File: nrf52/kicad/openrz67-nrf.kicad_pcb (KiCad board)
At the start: 2 copper layers, 27 x 29 mm, 13 parts, among them J1 Camera, J2 SWD, SW1 B3U-1000P, U1 E73-2G4M08S1C, U2 TLP172AM, U3 TLP172AM

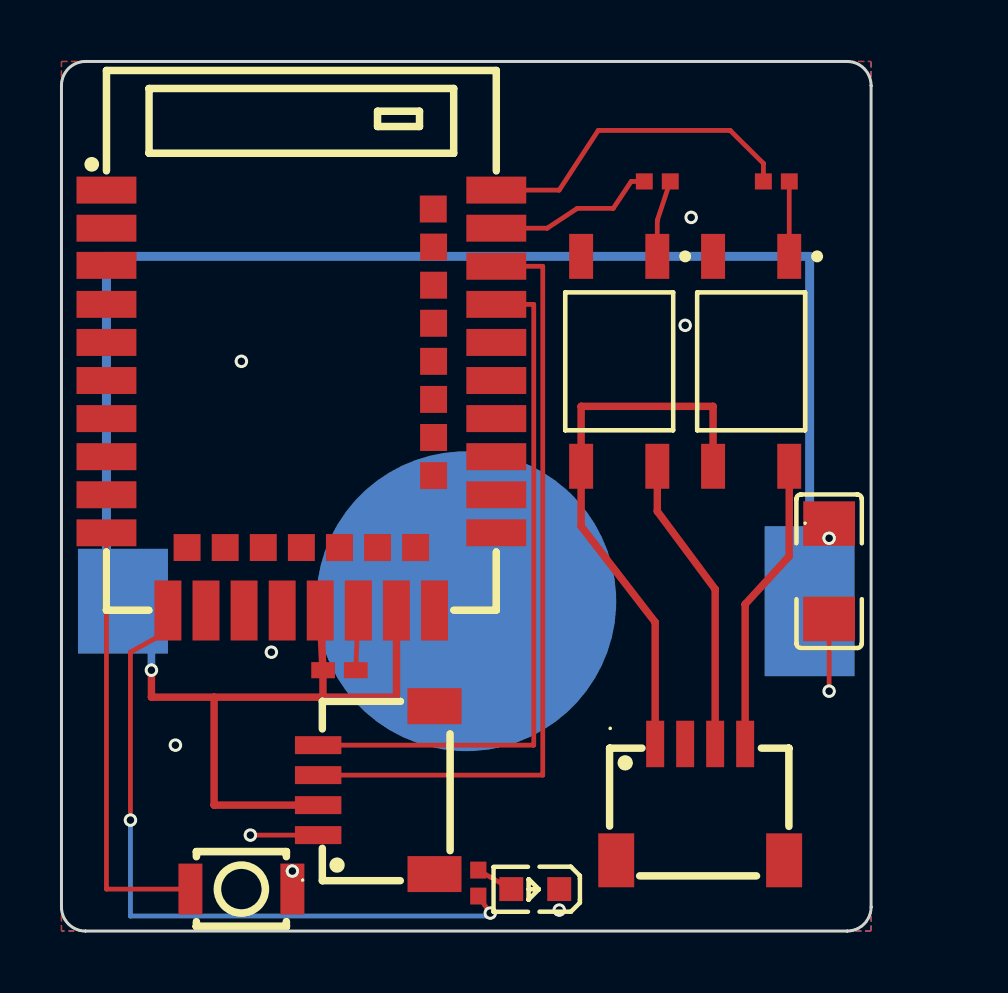
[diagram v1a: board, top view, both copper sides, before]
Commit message: nrf52: no paste on cell pad, VBUS to GND, vias out of pads
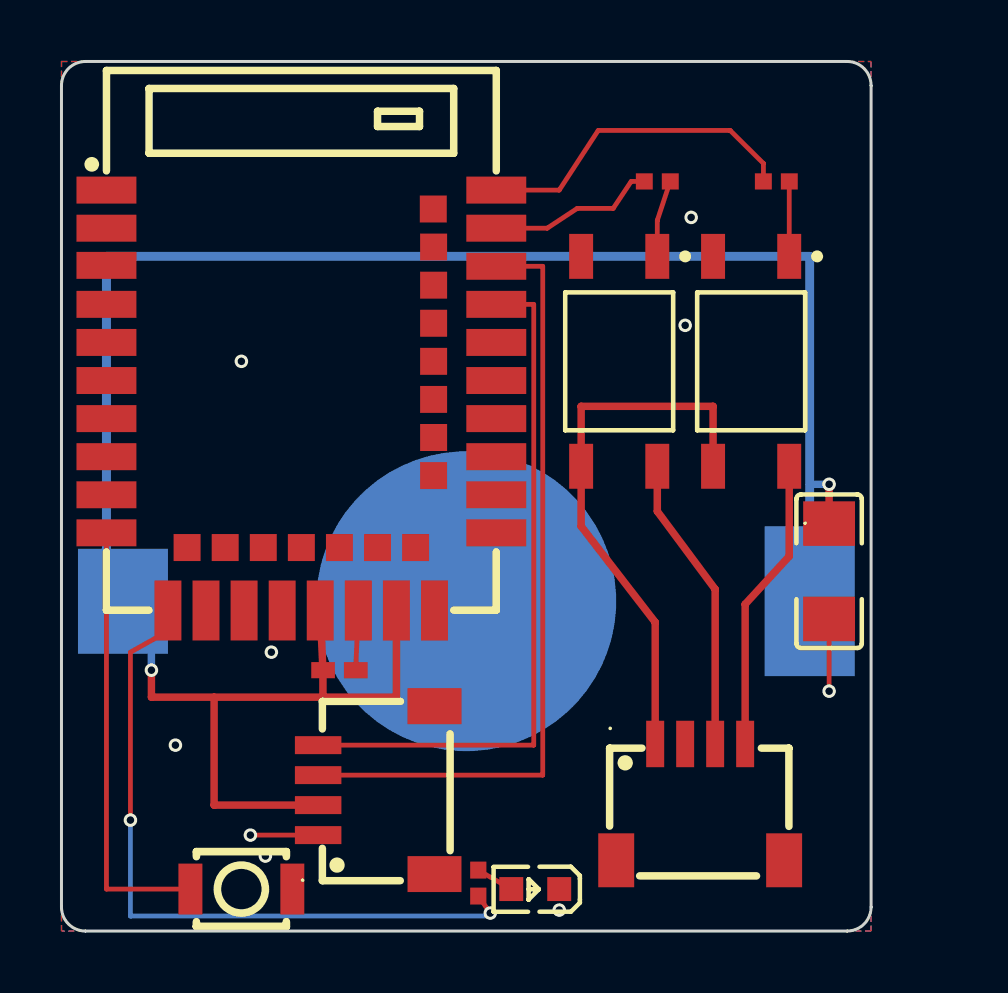
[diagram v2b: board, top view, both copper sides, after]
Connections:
- U1 pad 27: unconnected-(U1-VBS-Pad27) -> GND
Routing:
- net VDD: track 65.7 -> 67.2 mm

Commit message: nrf52 pcb: cell polarity label on the back silkscreen
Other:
- board text added: "CR2032 + SIDE OUT"

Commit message: nrf52 pcb: basic C2, R3 shares the 330 Ω part
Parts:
- R3: value 1kΩ -> 330Ω

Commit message: nrf52 pcb: connector names and board name on silkscreen
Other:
- board text added: "CAM"
- board text added: "OpenRZ67 nRF rev A"
- board text added: "SWD"

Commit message: nrf52 pcb: reverse-cell P-MOSFET
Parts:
- added Q1: AO3401A, openrz67-nrf:SOT-23, F.Cu at (5.40, 21.3)
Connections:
- BT1 pad 1: VDD -> VBAT
- BT1 pad 2: VDD -> VBAT
- C1 pad 1: VDD -> VBAT
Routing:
- net VDD: track 67.2 -> 16.1 mm, vias 2 -> 0
- net VBAT: track 0.00 -> 48.4 mm, vias 0 -> 2
- net GND: track 5.88 -> 6.56 mm

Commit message: nrf52: J2 mouth at the board edge, board 29.5 wide
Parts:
- moved R3 4.03 mm to (17.4, 25.4), turned to -90 degrees
- moved D1 2.40 mm to (18.2, 27.6)
- moved J1 2.30 mm to (23.6, 24.7)
- moved J2 1.84 mm to (12.3, 24.7), turned to 0 degrees
- moved C1 0.90 mm to (26.5, 17.0)
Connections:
- J2 pad 3: SWCLK -> SWDIO
- J2 pad 4: SWDIO -> SWCLK
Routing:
- net LED_DRV: track 23.7 -> 29.6 mm
- net SWCLK: track 25.2 -> 19.7 mm
- net SWDIO: track 22.4 -> 18.9 mm
- net VDD: track 16.1 -> 14.3 mm
- net CAM_GND: track 17.7 -> 19.5 mm
- net S1: track 9.14 -> 10.9 mm
- net GND: track 6.56 -> 5.08 mm, vias 9 -> 8
- net VBAT: track 48.4 -> 49.3 mm
- net S2: track 9.07 -> 9.61 mm
- net LED_A: track 1.27 -> 1.77 mm
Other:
- board size 27 x 29 mm -> 29.5 x 29 mm

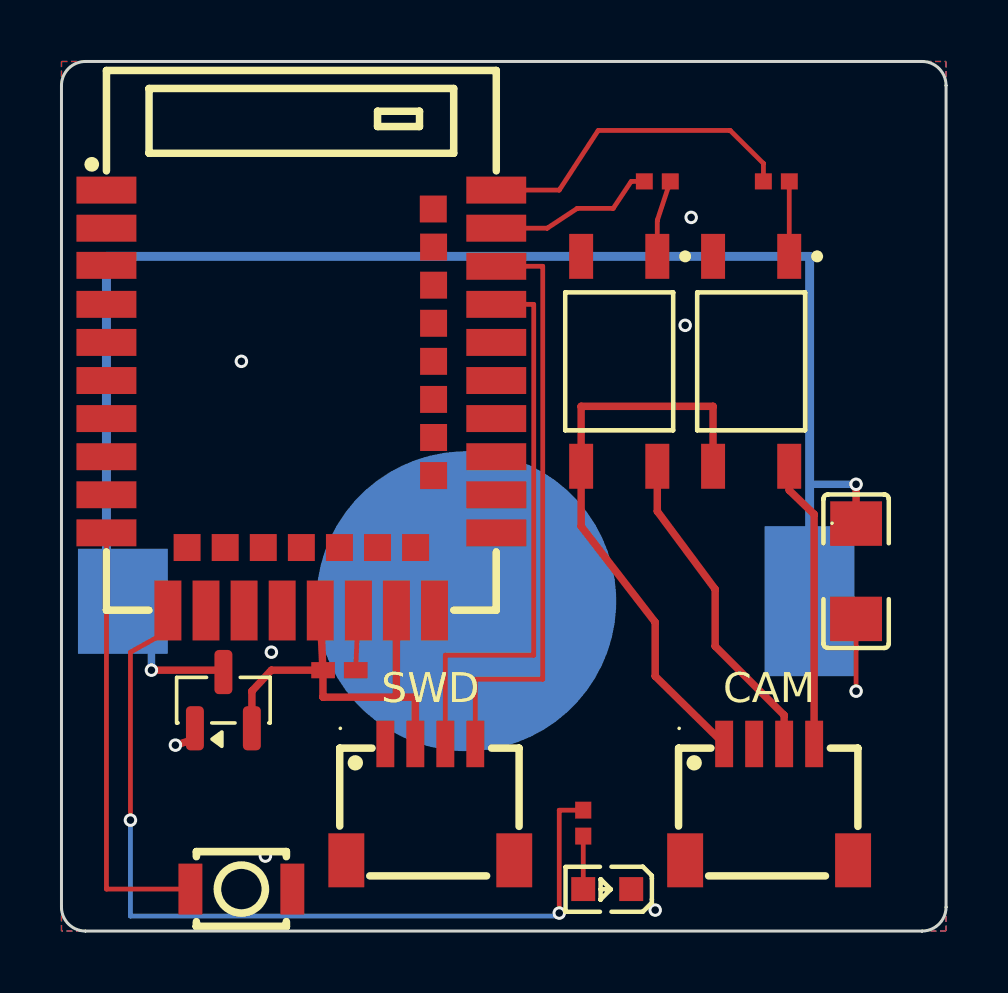
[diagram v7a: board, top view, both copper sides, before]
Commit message: nrf52 pcb: E73-2G4M08S1F (nRF54L15) module
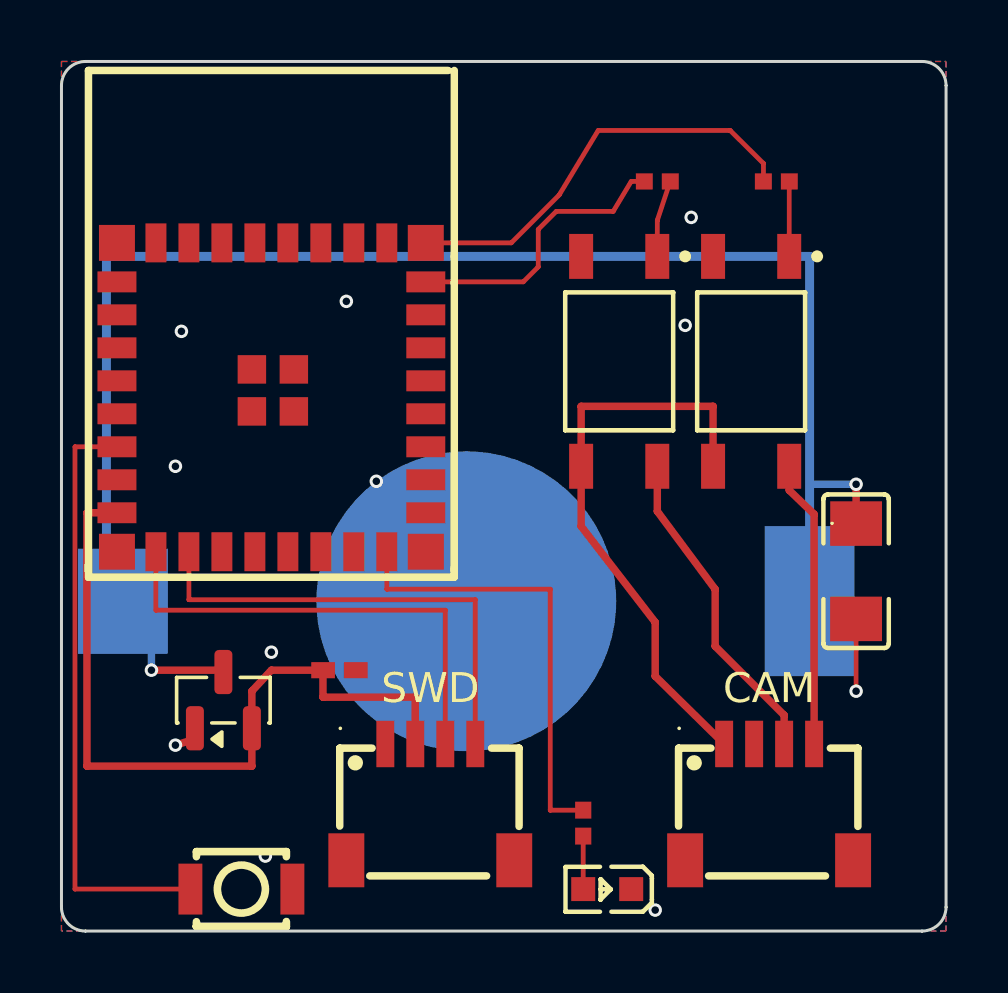
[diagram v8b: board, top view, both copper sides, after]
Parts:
- U1: value E73-2G4M08S1C -> E73-2G4M08S1F; footprint openrz67-nrf:WIRELM-SMD_E73-2G4M08S1C -> openrz67-nrf:WIRELM-SMD_E73-2G4M08S1F
- moved U1 1.00 mm to (7.00, 11.2), turned to 0 degrees
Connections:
- J2 pad 3: SWDIO -> SWCLK
- J2 pad 4: SWCLK -> SWDIO
- U1 pad 10: BTN -> GND
- U1 pad 11: LED_DRV -> SWCLK
- U1 pad 12: unconnected-(U1-P0.26-Pad12) -> SWDIO
- U1 pad 18: unconnected-(U1-AI2-Pad18) -> LED_DRV
- U1 pad 19: VDD -> unconnected-(U1-nRESET-Pad19)
- U1 pad 21: GND -> unconnected-(U1-P2.02-Pad21)
- U1 pad 23: VDD -> unconnected-(U1-P2.06-Pad23)
- U1 pad 24: GND -> unconnected-(U1-P2.08-Pad24)
- U1 pad 27: GND -> S1_DRV
- U1 pad 28: unconnected-(U1-P15-Pad28) -> S2_DRV
- U1 pad 30: unconnected-(U1-P17-Pad30) -> GND
- U1 pad 31: unconnected-(U1-D+-Pad31) -> GND
- U1 pad 37: SWDIO -> GND
- U1 pad 38: unconnected-(U1-P1.02-Pad38) -> GND
- U1 pad 39: SWCLK -> GND
- U1 pad 40: unconnected-(U1-P1.04-Pad40) -> GND
- U1 pad 5: GND -> unconnected-(U1-P1.13-Pad5)
- U1 pad 7: unconnected-(U1-AI0-Pad7) -> BTN
- U1 pad 9: unconnected-(U1-AI7-Pad9) -> VDD
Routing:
- net LED_DRV: track 29.6 -> 15.2 mm, vias 2 -> 0
- net VDD: track 14.3 -> 25.7 mm
- net BTN: track 14.7 -> 20.0 mm
- net S1_DRV: track 5.62 -> 9.56 mm
- net SWCLK: track 19.7 -> 16.1 mm
- net S2_DRV: track 11.0 -> 14.2 mm
- net SWDIO: track 18.9 -> 16.0 mm
- net GND: track 5.08 -> 3.09 mm, vias 8 -> 11
